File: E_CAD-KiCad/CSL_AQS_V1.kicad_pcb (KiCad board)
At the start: 2 copper layers, 165.1 x 54.6 mm, 262 parts, among them J2 Grove STEMMA, J3 Grove STEMMA

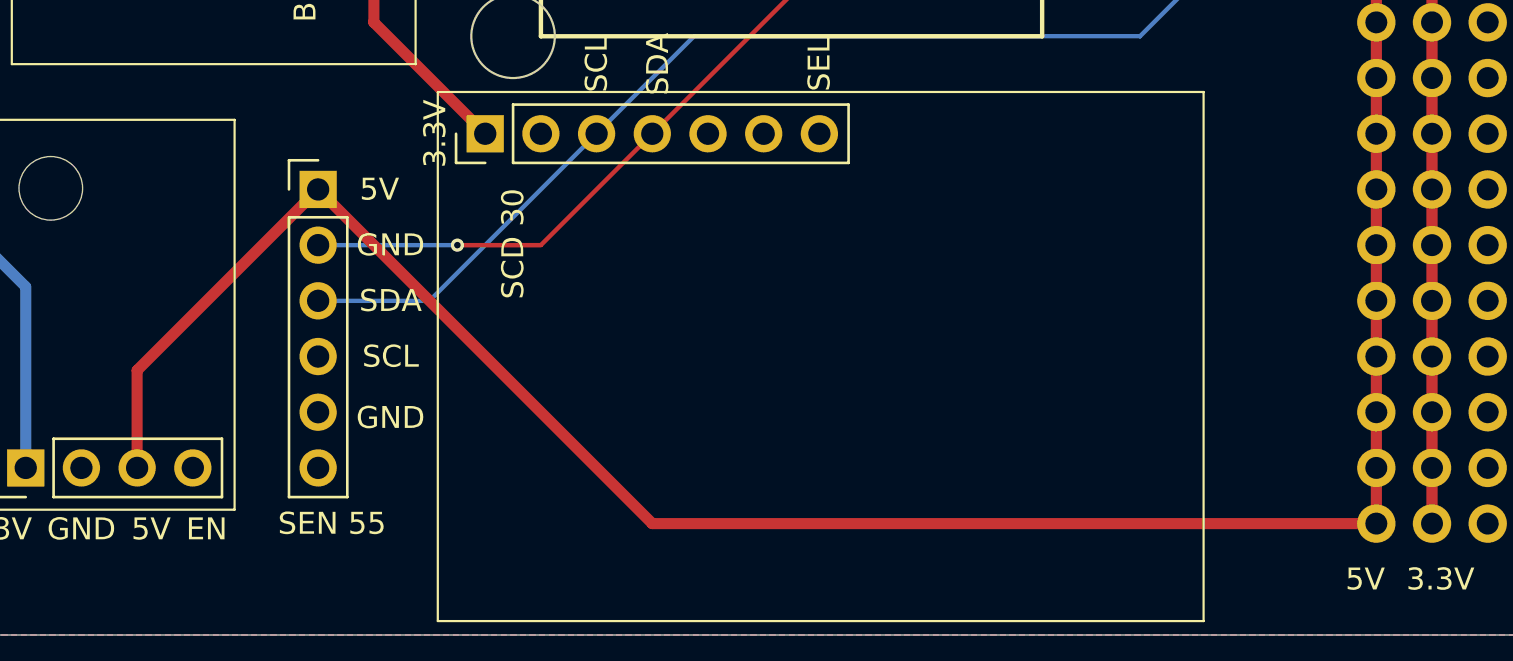
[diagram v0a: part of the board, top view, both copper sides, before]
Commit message: Update to Sen55 Pads
Made corrections to the misconnected pads of the Sen55
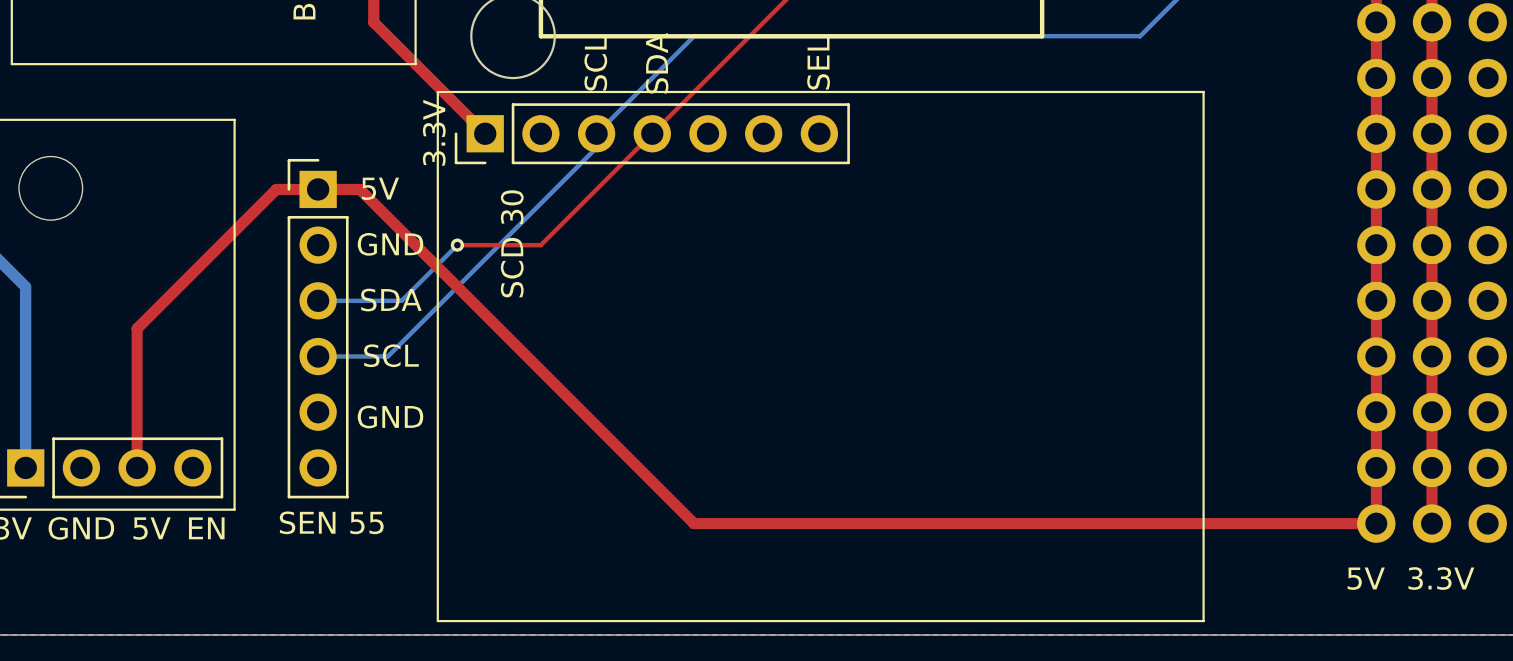
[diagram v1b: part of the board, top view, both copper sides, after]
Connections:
- JP8 pad 2: SDA -> GND
- JP8 pad 3: SCL -> SDA
- JP8 pad 4: GND -> SCL
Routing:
- net SCL: track 219.8 -> 221.2 mm
- net 5V: track 113.9 -> 115.0 mm
- net SDA: track 222.8 -> 223.9 mm
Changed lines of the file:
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@@
 			(layers "*.Cu" "*.Mask")
 			(remove_unused_layers no)
-			(net 21 "SDA")
+			(net 22 "GND")
 			(pinfunction "2")
 			(pintype "passive")
@@
 			(layers "*.Cu" "*.Mask")
 			(remove_unused_layers no)
-			(net 6 "SCL")
+			(net 21 "SDA")
 			(pinfunction "3")
 			(pintype "passive")
@@
 			(layers "*.Cu" "*.Mask")
 			(remove_unused_layers no)
-			(net 22 "GND")
+			(net 6 "SCL")
 			(pinfunction "4")
 			(pintype "passive")
@@
 	)
 	(segment
-		(start 137.16 96.52)
-		(end 129.54 104.14)
-		(width 0.2)
-		(layer "B.Cu")
-		(net 6)
-	)
-	(segment
 		(start 55.88 102.87)
 		(end 60.96 107.95)
@@
 	)
 	(segment
-		(start 165.862 88.916)
-		(end 165.1 88.916)
+		(start 127.635 106.68)
+		(end 124.46 106.68)
 		(width 0.2)
 		(layer "B.Cu")
@@
 	)
 	(segment
-		(start 129.54 104.14)
-		(end 124.46 104.14)
+		(start 165.862 88.916)
+		(end 165.1 88.916)
 		(width 0.2)
 		(layer "B.Cu")
@@
 	)
 	(segment
+		(start 137.16 97.155)
+		(end 127.635 106.68)
+		(width 0.2)
+		(layer "B.Cu")
+		(net 6)
+	)
+	(segment
+		(start 137.16 96.52)
+		(end 137.16 97.155)
+		(width 0.2)
+		(layer "B.Cu")
+		(net 6)
+	)
+	(segment
 		(start 81.28 76.2)
 		(end 59.055 76.2)
@@
 	)
 	(segment
+		(start 128.27 104.14)
+		(end 124.46 104.14)
+		(width 0.2)
+		(layer "B.Cu")
+		(net 21)
+	)
+	(segment
 		(start 55.245 104.775)
 		(end 55.245 73.025)
@@
 	)
 	(segment
-		(start 130.81 101.6)
-		(end 124.46 101.6)
-		(width 0.2)
-		(layer "B.Cu")
-		(net 21)
-	)
-	(segment
 		(start 55.245 73.025)
 		(end 56.515 71.755)
@@
 	)
 	(segment
+		(start 130.81 101.6)
+		(end 128.27 104.14)
+		(width 0.2)
+		(layer "B.Cu")
+		(net 21)
+	)
+	(segment
 		(start 58.42 107.95)
 		(end 55.245 104.775)
@@
 	)
 	(segment
-		(start 172.72 109.22)
-		(end 172.72 106.68)
+		(start 116.205 111.76)
+		(end 116.205 105.41)
 		(width 0.508)
 		(layer "F.Cu")
@@
 	)
 	(segment
-		(start 116.205 111.76)
-		(end 116.205 107.315)
+		(start 172.72 109.22)
+		(end 172.72 106.68)
 		(width 0.508)
 		(layer "F.Cu")
@@
 	)
 	(segment
+		(start 116.205 105.41)
+		(end 122.555 99.06)
+		(width 0.508)
+		(layer "F.Cu")
+		(net 45)
+	)
+	(segment
+		(start 122.555 99.06)
+		(end 124.46 99.06)
+		(width 0.508)
+		(layer "F.Cu")
+		(net 45)
+	)
+	(segment
+		(start 141.605 114.3)
+		(end 126.365 99.06)
+		(width 0.508)
+		(layer "F.Cu")
+		(net 45)
+	)
+	(segment
 		(start 172.72 83.82)
 		(end 172.72 81.28)
@@
 	)
 	(segment
-		(start 116.205 107.315)
-		(end 124.46 99.06)
-		(width 0.508)
-		(layer "F.Cu")
-		(net 45)
-	)
-	(segment
 		(start 172.72 104.14)
 		(end 172.72 101.6)
@@
 	(segment
 		(start 172.72 114.3)
-		(end 139.7 114.3)
+		(end 141.605 114.3)
 		(width 0.508)
 		(layer "F.Cu")
@@
 	)
 	(segment
-		(start 139.7 114.3)
+		(start 126.365 99.06)
 		(end 124.46 99.06)
 		(width 0.508)

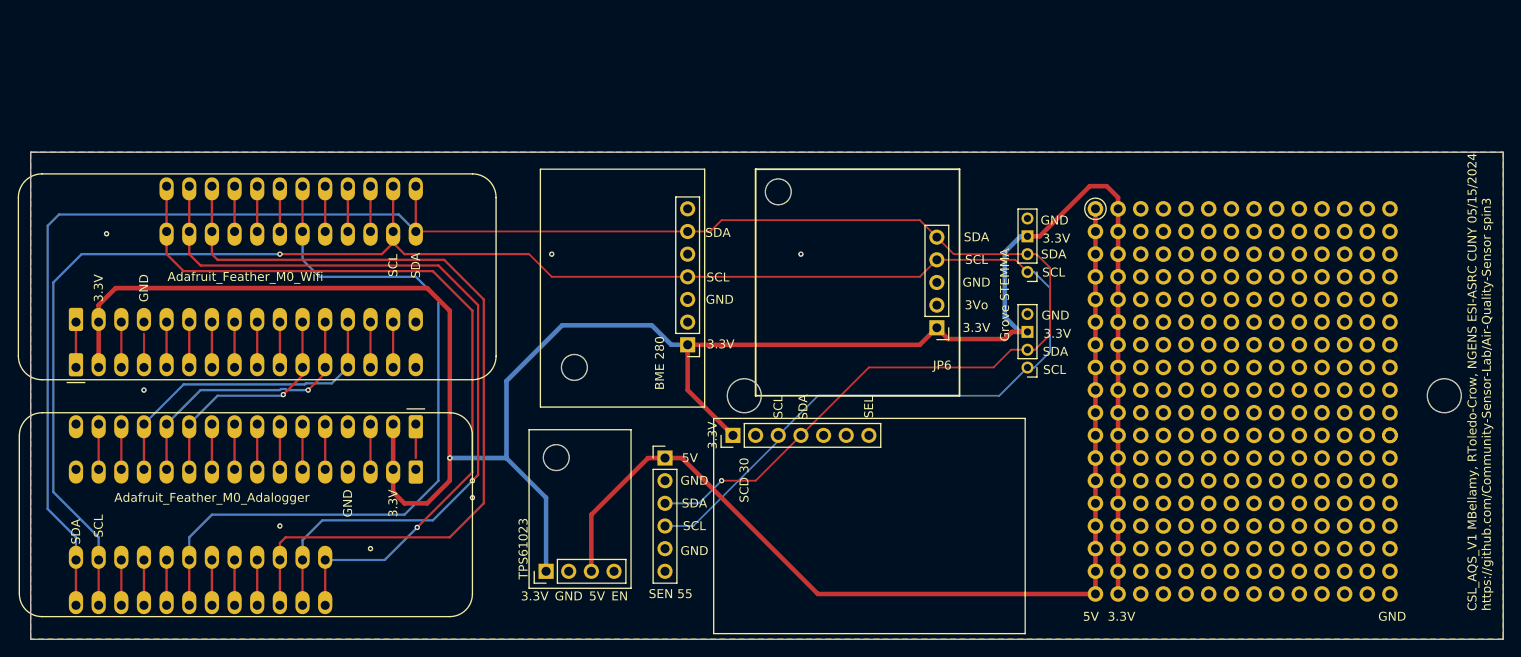
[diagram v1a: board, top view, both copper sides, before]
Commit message: Corrections to PCB Board Connections
Connected the required pads to function the buttons on the microcontroller and logger when stacked together
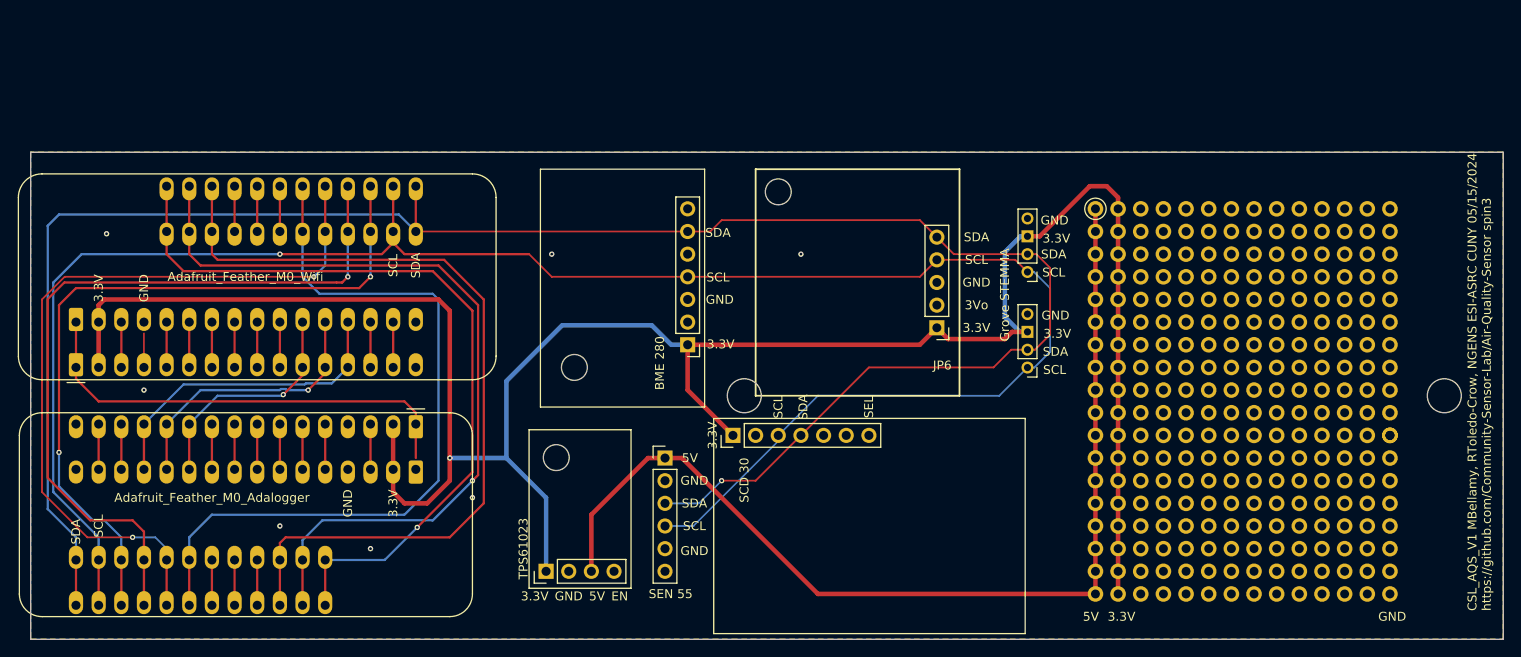
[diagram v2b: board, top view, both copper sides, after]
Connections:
- A1 pad 1: unconnected-(A1-~{RESET}-Pad1) -> Net-(A1-~{RESET})
- A1 pad 19: unconnected-(A1-D5-Pad19) -> Net-(A1-D5)
- A1 pad 20: unconnected-(A1-D6-Pad20) -> Net-(A1-D6)
- A1 pad 21: unconnected-(A1-D9-Pad21) -> Net-(A1-D9)
- A2 pad 1: unconnected-(A2-~{RESET}-Pad1) -> Net-(A1-~{RESET})
- A2 pad 19: unconnected-(A2-D5-Pad19) -> Net-(A1-D5)
- A2 pad 20: unconnected-(A2-D6-Pad20) -> Net-(A1-D6)
- A2 pad 21: unconnected-(A2-D9-Pad21) -> Net-(A1-D9)
- JP8 pad 2: GND -> SDA
- JP8 pad 3: SDA -> SCL
- JP8 pad 4: SCL -> GND
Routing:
- net Net-(A1-D9): track 0.00 -> 86.8 mm, vias 0 -> 2
- net Net-(A1-D6): track 0.00 -> 86.4 mm, vias 0 -> 1
- net Net-(A1-D5): track 0.00 -> 83.7 mm, vias 0 -> 2
- net Net-(A1-~{RESET}): track 0.00 -> 51.1 mm
- net unconnected-(A1-~{RESET}-Pad1): track 5.08 -> 0.00 mm
- net unconnected-(A2-D9-Pad21): track 5.08 -> 0.00 mm
- net unconnected-(A2-D6-Pad20): track 5.08 -> 0.00 mm
- net unconnected-(A2-D5-Pad19): track 5.08 -> 0.00 mm
- net unconnected-(A1-D9-Pad21): track 5.08 -> 0.00 mm
- net unconnected-(A1-D6-Pad20): track 5.08 -> 0.00 mm
- net unconnected-(A1-D5-Pad19): track 5.08 -> 0.00 mm
- net unconnected-(A2-~{RESET}-Pad1): track 3.81 -> 0.00 mm
- net Net-(A1-D10): track 84.4 -> 85.5 mm
- net 3.3V: track 259.4 -> 258.4 mm
